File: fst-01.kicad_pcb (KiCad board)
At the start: 2 copper layers, 21.2 x 12.6 mm, 19 parts, among them J1 USB_A, K1 CONN_3, U1 STM32F103TB, U2 MCP1700-3302E, U3 NUF2221W1, U4 X2SON, X1 12MHz

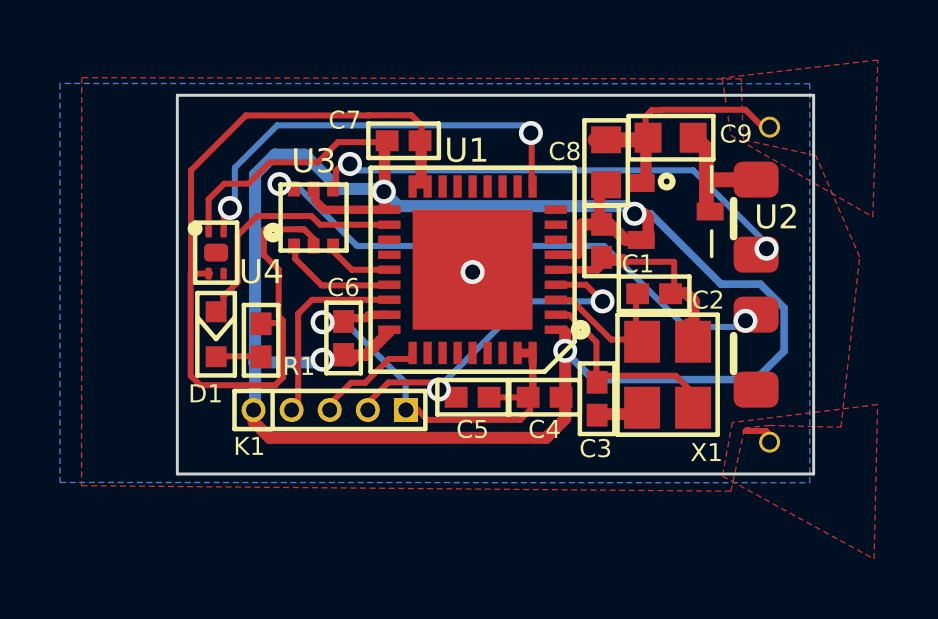
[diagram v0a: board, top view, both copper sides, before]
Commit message: change parts.
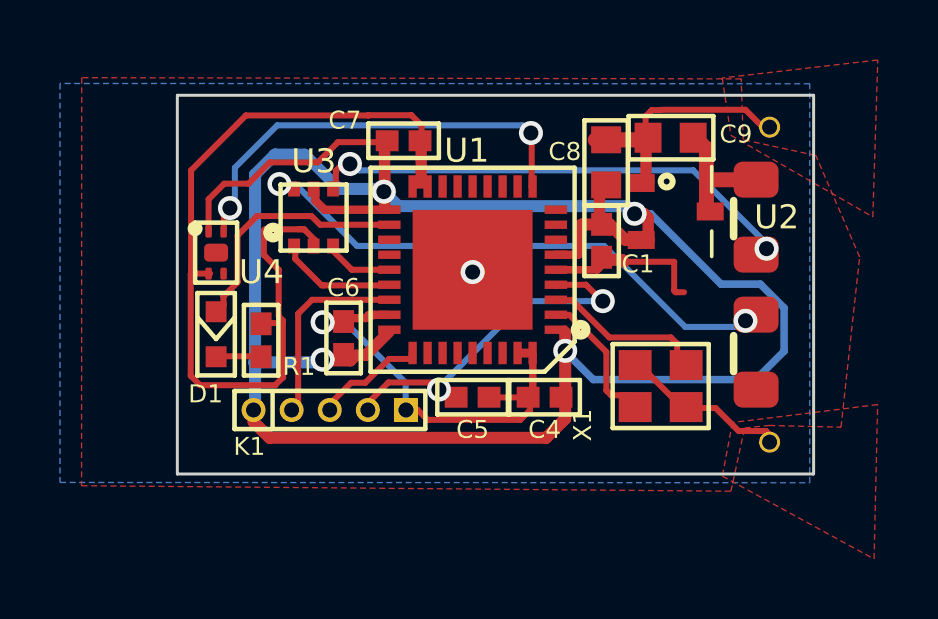
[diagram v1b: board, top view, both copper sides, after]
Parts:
- removed C2, C3: 27pF, FST:c_0402
- R1: value 510 -> 470
- X1: footprint FST:ABM8G -> FST:FA-20H
- moved X1 0.44 mm to (124.6, 102.4), turned to 0 degrees
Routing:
- net /OSC_IN: track 7.03 -> 4.94 mm
- net GND: track 74.1 -> 75.4 mm
- net /OSC_OUT: track 5.97 -> 5.30 mm

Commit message: Ask PCBA quote with this.
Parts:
- moved C7 5.56 mm to (124.9, 99.7)
- renumbered C4 to C2, C5 to C3, C6 to C4, C7 to C5, C8 to C6, C9 to C7
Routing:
- net GND: track 75.4 -> 74.1 mm
- net /VBUS: track 3.93 -> 4.65 mm

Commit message: Add position file and name change for U1 to GD.
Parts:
- U1: value STM32F103TB -> GD32F103TB
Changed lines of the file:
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@@
       (effects (font (size 0.8001 0.8001) (thickness 0.1524)))
     )
-    (fp_text value STM32F103TB (at -0.0254 2.0955 180) (layer F.SilkS) hide
+    (fp_text value GD32F103TB (at -0.0254 2.0955 180) (layer F.SilkS) hide
       (effects (font (size 0.508 0.508) (thickness 0.0762)))
     )

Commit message: Update PCBA.
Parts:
- K1: value CONN_3 -> CONN_5
- U4: value X2SON -> DRV5032FA
- moved U4 0.07 mm to (109.8, 98.0)
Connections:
- U4 pad 3: (no net) -> Net-(U4-Pad3)
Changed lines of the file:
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@@
     (zones 0)
     (modules 17)
-    (nets 33)
+    (nets 34)
   )
   (page A4)
@@
   (net 31 "Net-(U1-Pad14)")
   (net 32 /PA3)
+  (net 33 "Net-(U4-Pad3)")
   (net_class Default "This is the default net class."
     (clearance 0.20066)
@@
     (add_net "Net-(U1-Pad8)")
     (add_net "Net-(U1-Pad9)")
+    (add_net "Net-(U4-Pad3)")
   )
   (net_class GND ""
@@
     (uvia_drill 0.14986)
   )
+  (module FST:X2SON (layer Front)
+    (at 109.75 97.9965)
+    (attr smd)
+    (fp_text reference U4 (at 1.5782 0.8887) (layer F.SilkS)
+      (effects (font (size 0.8 0.8) (thickness 0.15)))
+    )
+    (fp_text value DRV5032FA (at 0 -4.6) (layer F.Fab)
+      (effects (font (size 1 1) (thickness 0.15)))
+    )
+    (fp_line (start -0.55 -0.25) (end -0.1 -0.7) (layer Dwgs.User) (width 0.15))
+    (fp_circle (center -0.7 -0.8) (end -0.7 -0.7) (layer F.SilkS) (width 0.3))
+    (fp_line (start -0.7 -1) (end 0.7 -1) (layer F.SilkS) (width 0.15))
+    (fp_line (start 0.7 -1) (end 0.7 1) (layer F.SilkS) (width 0.15))
+    (fp_line (start 0.7 1) (end -0.7 1) (layer F.SilkS) (width 0.15))
+    (fp_line (start -0.7 1) (end -0.7 -1) (layer F.SilkS) (width 0.15))
+    (fp_line (start -0.55 -0.7) (end 0.55 -0.7) (layer Dwgs.User) (width 0.15))
+    (fp_line (start -0.55 0.7) (end 0.55 0.7) (layer Dwgs.User) (width 0.15))
+    (fp_line (start -0.55 -0.7) (end -0.55 0.7) (layer Dwgs.User) (width 0.15))
+    (fp_line (start 0.55 -0.7) (end 0.55 0.7) (layer Dwgs.User) (width 0.15))
+    (pad 5 smd roundrect (at 0 0) (size 0.8 0.6) (layers Front F.Paste F.Mask) (roundrect_rratio 0.25)
+      (solder_mask_margin 0.05) (solder_paste_margin -0.05) (clearance 0.05))
+    (pad 1 smd roundrect (at -0.25 -0.7) (size 0.22 0.4) (layers Front F.Paste F.Mask) (roundrect_rratio 0.25)
+      (net 13 +3V3) (solder_mask_margin 0.05) (clearance 0.05))
+    (pad 4 smd roundrect (at 0.25 -0.7) (size 0.22 0.4) (layers Front F.Paste F.Mask) (roundrect_rratio 0.25)
+      (net 32 /PA3) (solder_mask_margin 0.05) (clearance 0.05))
+    (pad 2 smd roundrect (at -0.25 0.7) (size 0.22 0.4) (layers Front F.Paste F.Mask) (roundrect_rratio 0.25)
+      (net 12 GND) (solder_mask_margin 0.05) (clearance 0.05))
+    (pad 3 smd roundrect (at 0.25 0.7) (size 0.22 0.4) (layers Front F.Paste F.Mask) (roundrect_rratio 0.25)
+      (net 33 "Net-(U4-Pad3)") (solder_mask_margin 0.05) (clearance 0.05))
+  )
   (module FST:SOT-23 (layer Front)
-    (at 125.0696 96.5581)
+    (at 125.07 96.5565)
     (descr "SOT-23, Standard")
     (tags SOT-23)
@@
   )
   (module FST:SOT363 (layer Front)
-    (at 113 96.76)
+    (at 113 96.7565)
     (descr "SMALL OUTLINE TRANSISTOR")
     (tags "SMALL OUTLINE TRANSISTOR")
@@
   )
   (module FST:FA-20H (layer Front)
-    (at 124.56922 102.37724)
+    (at 124.57 102.3765)
     (attr smd)
     (fp_text reference X1 (at 0.01778 1.97866) (layer F.SilkS)
@@
   )
   (module FST:LED0603 (layer Front)
-    (at 109.75 100.65 270)
+    (at 109.75 100.6565 270)
     (descr "LED 0603 smd package")
     (tags "LED led 0603 SMD smd SMT smt smdled SMDLED smtled SMTLED")
@@
       (effects (font (size 0.6 0.6) (thickness 0.15)))
     )
-    (fp_text value CONN_3 (at 0 -2.159) (layer F.SilkS) hide
+    (fp_text value CONN_5 (at 0 -2.159) (layer F.SilkS) hide
       (effects (font (size 1.016 1.016) (thickness 0.1524)))
     )
@@
   )
   (module FST:QFN36 (layer Front)
-    (at 118.3 98.5 180)
+    (at 118.3 98.5065 180)
     (descr "Support QFN 36 pins")
     (tags QFN36)
@@
       (net 12 GND) (solder_mask_margin 0.05) (solder_paste_margin -0.4699))
   )
-  (module FST:X2SON (layer Front)
-    (at 109.75 97.93)
-    (fp_text reference U4 (at 1.5782 0.8887) (layer F.SilkS)
-      (effects (font (size 0.8 0.8) (thickness 0.15)))
-    )
-    (fp_text value X2SON (at 0 -4.6) (layer F.Fab)
-      (effects (font (size 1 1) (thickness 0.15)))
-    )
-    (fp_line (start 0.55 -0.7) (end 0.55 0.7) (layer Dwgs.User) (width 0.15))
-    (fp_line (start -0.55 -0.7) (end -0.55 0.7) (layer Dwgs.User) (width 0.15))
-    (fp_line (start -0.55 0.7) (end 0.55 0.7) (layer Dwgs.User) (width 0.15))
-    (fp_line (start -0.55 -0.7) (end 0.55 -0.7) (layer Dwgs.User) (width 0.15))
-    (fp_line (start -0.7 1) (end -0.7 -1) (layer F.SilkS) (width 0.15))
-    (fp_line (start 0.7 1) (end -0.7 1) (layer F.SilkS) (width 0.15))
-    (fp_line (start 0.7 -1) (end 0.7 1) (layer F.SilkS) (width 0.15))
-    (fp_line (start -0.7 -1) (end 0.7 -1) (layer F.SilkS) (width 0.15))
-    (fp_circle (center -0.7 -0.8) (end -0.7 -0.7) (layer F.SilkS) (width 0.3))
-    (fp_line (start -0.55 -0.25) (end -0.1 -0.7) (layer Dwgs.User) (width 0.15))
-    (pad 3 smd roundrect (at 0.25 0.7) (size 0.22 0.4) (layers Front F.Paste F.Mask) (roundrect_rratio 0.25)
-      (solder_mask_margin 0.05) (clearance 0.05))
-    (pad 2 smd roundrect (at -0.25 0.7) (size 0.22 0.4) (layers Front F.Paste F.Mask) (roundrect_rratio 0.25)
-      (net 12 GND) (solder_mask_margin 0.05) (clearance 0.05))
-    (pad 4 smd roundrect (at 0.25 -0.7) (size 0.22 0.4) (layers Front F.Paste F.Mask) (roundrect_rratio 0.25)
-      (net 32 /PA3) (solder_mask_margin 0.05) (clearance 0.05))
-    (pad 1 smd roundrect (at -0.25 -0.7) (size 0.22 0.4) (layers Front F.Paste F.Mask) (roundrect_rratio 0.25)
-      (net 13 +3V3) (solder_mask_margin 0.05) (clearance 0.05))
-    (pad 5 smd roundrect (at 0 0) (size 0.8 0.6) (layers Front F.Paste F.Mask) (roundrect_rratio 0.25)
-      (solder_mask_margin 0.05) (solder_paste_margin -0.05) (clearance 0.05))
-  )
   (module FST:r_0402 (layer Front)
-    (at 111.25 100.85 270)
+    (at 111.25 100.8565 270)
     (descr "SMT resistor, 0402")
     (attr smd)
@@
   )
   (module FST:c_0603 (layer Front)
-    (at 124.9 99.6569)
+    (at 124.9 99.6565)
     (descr "SMT capacitor, 0603")
     (attr smd)
@@
   )
   (module FST:c_0402 (layer Front)
-    (at 122.6 97.536 270)
+    (at 122.6 97.5365 270)
     (descr "SMT capacitor, 0402")
     (attr smd)
@@
   )
   (module FST:c_0402 (layer Front)
-    (at 120.7 102.75 180)
+    (at 120.7 102.7565 180)
     (descr "SMT capacitor, 0402")
     (attr smd)
@@
   )
   (module FST:c_0402 (layer Front)
-    (at 116 94.2)
+    (at 116 94.2065)
     (descr "SMT capacitor, 0402")
     (attr smd)
@@
   )
   (module FST:c_0402 (layer Front)
-    (at 114 100.7745 90)
+    (at 114 100.7765 90)
     (descr "SMT capacitor, 0402")
     (attr smd)
@@
   )
   (module FST:c_0402 (layer Front)
-    (at 118.3 102.75 180)
+    (at 118.3 102.7565 180)
     (descr "SMT capacitor, 0402")
     (attr smd)
@@
   )
   (module FST:c_0603 (layer Front)
-    (at 122.75 94.92 270)
+    (at 122.75 94.8965 270)
     (descr "SMT capacitor, 0603")
     (attr smd)
@@
   (segment (start 112.9284 96.7105) (end 113.217831 96.999931) (width 0.20066) (layer Front) (net 5))
   (segment (start 110.4646 97.3582) (end 111.1123 96.7105) (width 0.20066) (layer Front) (net 5))
-  (segment (start 110.4646 98.9203) (end 110.4646 98.8822) (width 0.20066) (layer Front) (net 5))
-  (segment (start 109.9947 99.3902) (end 110.4646 98.9203) (width 0.20066) (layer Front) (net 5))
+  (segment (start 110.4646 98.9965) (end 110.4646 98.8822) (width 0.20066) (layer Front) (net 5))
+  (segment (start 109.9947 99.4664) (end 110.4646 98.9965) (width 0.20066) (layer Front) (net 5))
   (segment (start 109.8169 99.8728) (end 109.9947 99.695) (width 0.20066) (layer Front) (net 5))
-  (segment (start 109.9947 99.695) (end 109.9947 99.3902) (width 0.20066) (layer Front) (net 5))
+  (segment (start 109.9947 99.695) (end 109.9947 99.4664) (width 0.20066) (layer Front) (net 5))
   (segment (start 121.040808 99.001451) (end 121.090337 99.05098) (width 0.20066) (layer Front) (net 6) (status 30))
   (segment (start 121.040808 99.001451) (end 122.079891 99.001451) (width 0.20066) (layer Front) (net 6))
@@
   (segment (start 111.0488 95.32366) (end 111.71428 94.65818) (width 0.4) (layer Back) (net 13))
   (segment (start 111.05388 103.1875) (end 111.0488 103.18242) (width 0.4) (layer Back) (net 13))
-  (segment (start 111.0488 103.18242) (end 111.0488 95.32366) (width 0.4) (layer Back) (net 13))
+  (segment (start 111.0488 103.18242) (end 111.0488 95.31966) (width 0.4) (layer Back) (net 13))
   (segment (start 109.4994 96.1517) (end 109.4994 97.2185) (width 0.20066) (layer Front) (net 13))
   (segment (start 110.0201 95.631) (end 109.4994 96.1517) (width 0.20066) (layer Front) (net 13))
